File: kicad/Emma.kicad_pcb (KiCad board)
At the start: 4 copper layers, 55 x 35 mm, 78 parts, among them U1 ByA 100nF +3V3 U1-VDDA Bypass, U1 ByB 100nF +3V3 U1-VDD Bypass

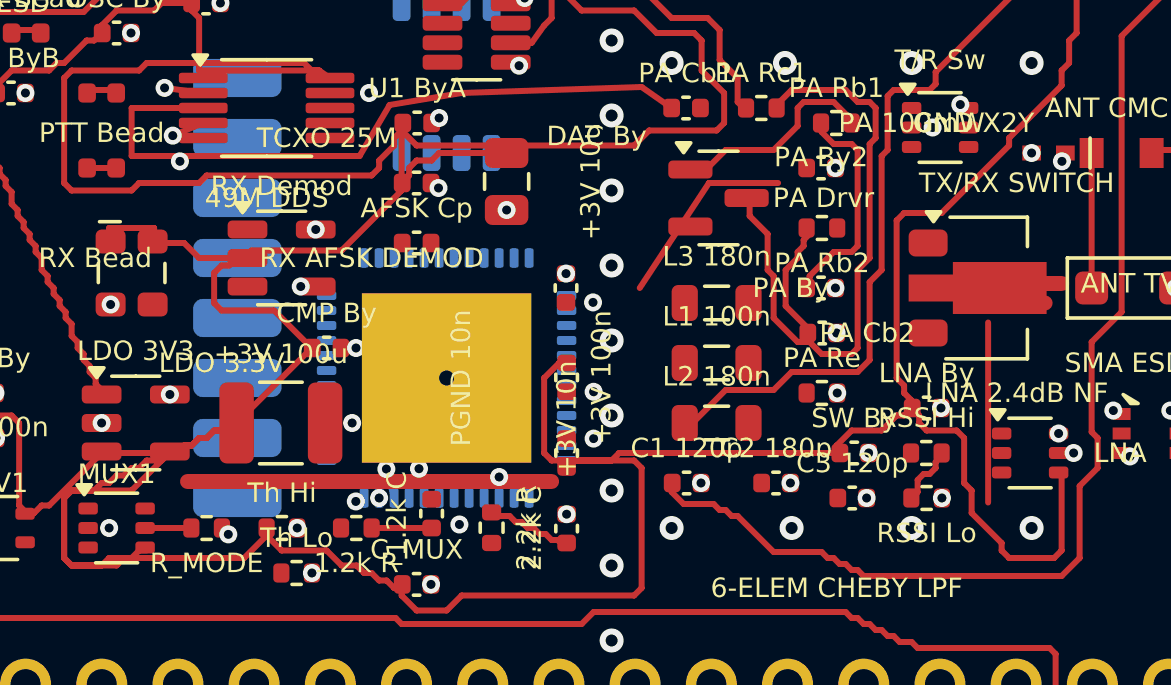
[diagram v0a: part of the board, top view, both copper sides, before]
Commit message: Clear Emma pre-existing DRC debt + schematic-parity so CI validator passes
Editing Emma.kicad_pcb pulled it into the CI KiCad validator's --changed-since
scope, which surfaced 35 pre-existing hard DRC violations plus 26 new
schematic-parity conflicts. All fixed at root cause (validator now reports
0 hard for Emma.kicad_sch ERC and Emma.kicad_pcb DRC):

- Schematic parity (26 net_conflict): gen_emma_sch.py now emits GLOBAL labels
  (bare net names match the PCB; local labels were named "/GND"). mod_emma_pcb.py
  assigns net-less pads the canonical "unconnected-(REF-PadN)" nets that the
  schematic no-connects generate.
- Solder-mask bridges (20): board solder-mask expansion was 0.10 mm (~2x normal),
  overlapping adjacent mask openings on 0.5 mm-pitch parts. cleanup_emma_drc.py
  sets it to the standard 0.05 mm.
- Clearance (15): POWER netclass clearance 0.20 -> 0.10 mm in Emma.kicad_pro
  (0.20 mm was over-conservative for a 5 V/3.3 V board and impossible for standard
  fine-pitch pads); the 4 real too-close auto-routed GND tracks deleted as
  redundant with the In1.Cu GND plane (GND connectivity unchanged: 23 -> 22
  unconnected).

Also black-formats cleanup_emma_drc.py; adds it to PROJECT_INDEX.md; updates
TODO.md. sch<->pcb parity remains exact.

Co-Authored-By: Claude Opus 4.8 <noreply@anthropic.com>
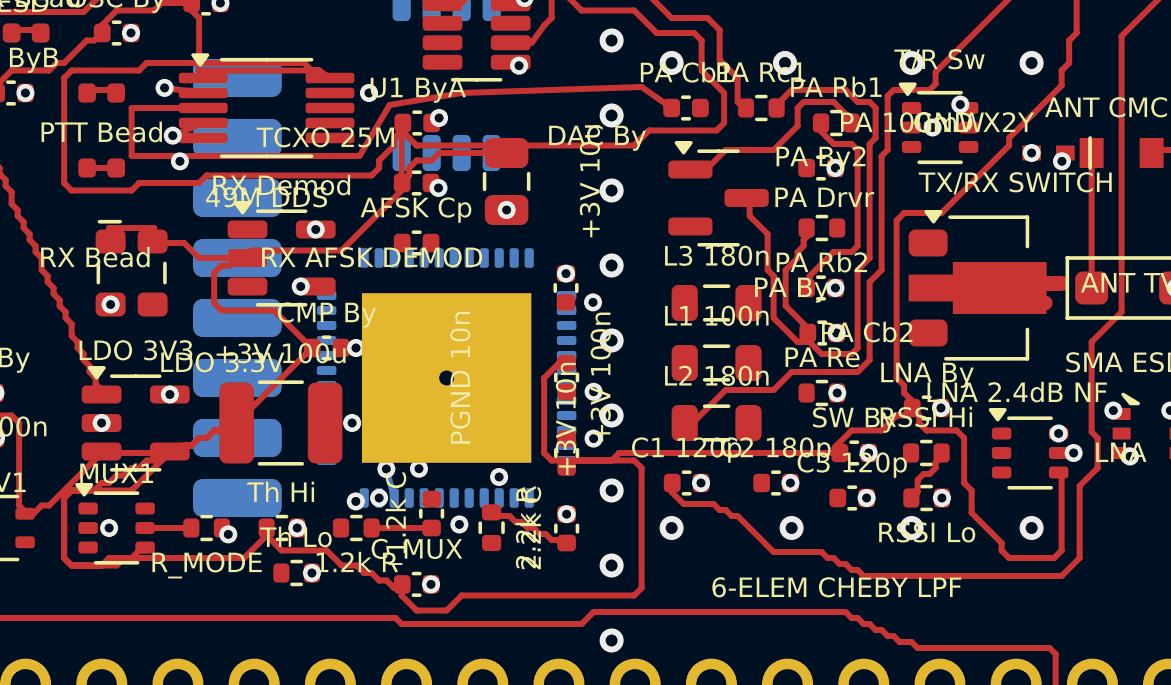
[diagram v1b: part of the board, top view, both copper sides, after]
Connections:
- ETH-PHY pad 13: (no net) -> unconnected-(ETH-PHY-Pad13)
- ETH-PHY pad 14: (no net) -> unconnected-(ETH-PHY-Pad14)
- ETH-PHY pad 15: (no net) -> unconnected-(ETH-PHY-Pad15)
- ETH-PHY pad 16: (no net) -> unconnected-(ETH-PHY-Pad16)
- ETH-PHY pad 17: (no net) -> unconnected-(ETH-PHY-Pad17)
- ETH-PHY pad 23: (no net) -> unconnected-(ETH-PHY-Pad23)
- ETH-PHY pad 24: (no net) -> unconnected-(ETH-PHY-Pad24)
- ETH-PHY pad 37: (no net) -> unconnected-(ETH-PHY-Pad37)
- ETH-PHY pad 38: (no net) -> unconnected-(ETH-PHY-Pad38)
- ETH-PHY pad 39: (no net) -> unconnected-(ETH-PHY-Pad39)
- ETH-PHY pad 42: (no net) -> unconnected-(ETH-PHY-Pad42)
- ETH-PHY pad 43: (no net) -> unconnected-(ETH-PHY-Pad43)
- ETH-PHY pad 44: (no net) -> unconnected-(ETH-PHY-Pad44)
- ETH-PHY pad 45: (no net) -> unconnected-(ETH-PHY-Pad45)
- ETH-PHY pad 46: (no net) -> unconnected-(ETH-PHY-Pad46)
- ETH-PHY pad 47: (no net) -> unconnected-(ETH-PHY-Pad47)
- ETH-PHY pad 48: (no net) -> unconnected-(ETH-PHY-Pad48)
- INV1 pad 5: (no net) -> unconnected-(INV1-Pad5)
- LoRa pad 11: (no net) -> unconnected-(LoRa-Pad11)
- LoRa pad 12: (no net) -> unconnected-(LoRa-Pad12)
- LoRa pad 13: (no net) -> unconnected-(LoRa-Pad13)
- LoRa pad 14: (no net) -> unconnected-(LoRa-Pad14)
- LoRa pad 15: (no net) -> unconnected-(LoRa-Pad15)
- LoRa pad 16: (no net) -> unconnected-(LoRa-Pad16)
- LoRa pad 7: (no net) -> unconnected-(LoRa-Pad7)
- LoRa pad 9: (no net) -> unconnected-(LoRa-Pad9)
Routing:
- net GND: track 33.9 -> 9.27 mm
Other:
- rule pad_to_mask_clearance: 0.1 -> 0.05

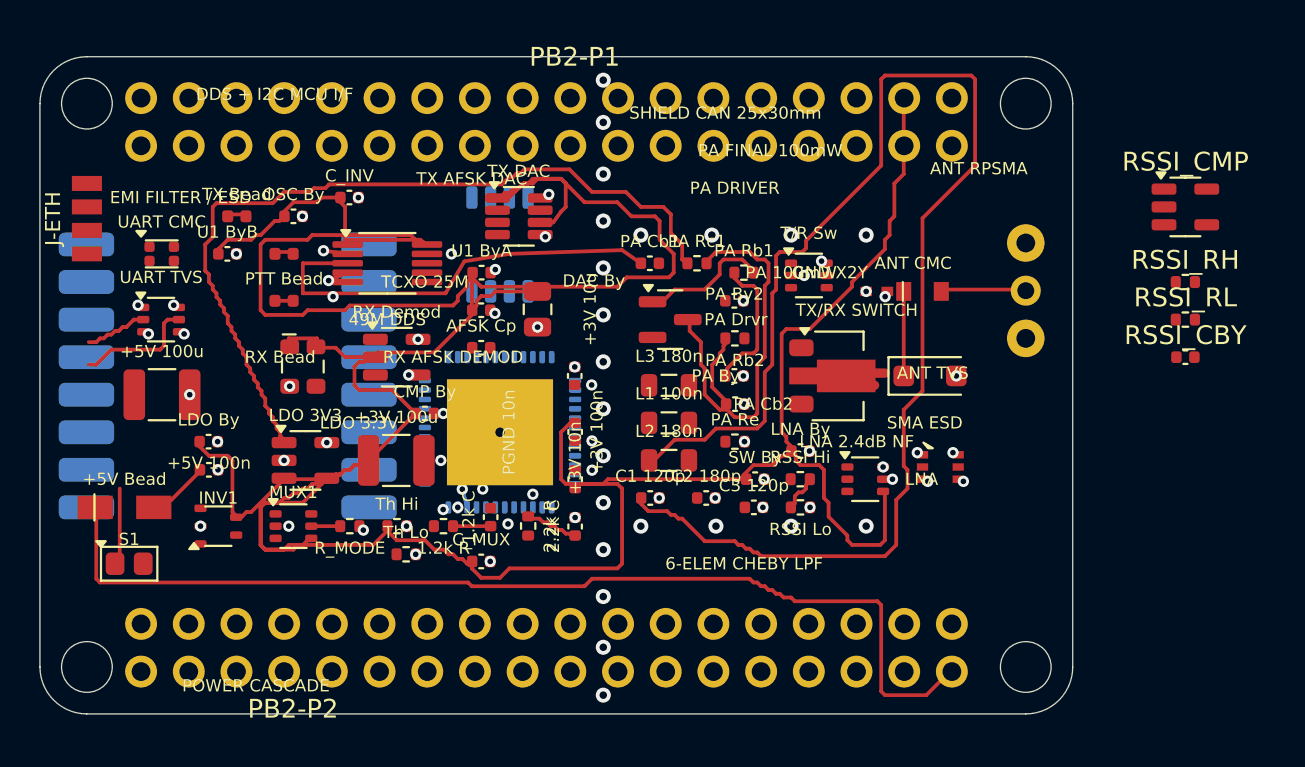
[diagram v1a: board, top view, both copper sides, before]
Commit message: Emma: route RSSI sub-circuit after user placement (0 hard DRC)
The user manually placed the 4 RSSI parts (RSSI_CMP + RSSI_RH/RL/CBY) on B.Cu in
the RF section and marked "NET validation, DRC & Routing" as the next step.

- Validated: sch<->pcb parity exact (refs + net sets match); the placement
  introduced 0 hard DRC violations (0 shorting/clearance/courtyard/solder-mask).
- Routed the sub-circuit via avionics/kicad/route_emma_rssi.py (pcbnew), DRC-tuned:
    GND      -> B.Cu tie of the 3 GND pads + one via to the F.Cu GND pour at RL.2
    RSSI_REF -> B.Cu weave through the 0.5 mm mid-channel around the wide CMP.4 pad
    +3V3     -> internal (RH.1/CBY.1/CMP.2) + board tie to LNA By
    RSSI_ANA -> CMP.1 -> RSSI Lo divider (B.Cu east + via)
  0.15 mm traces, 0.30 mm-drill/0.55 mm vias, zones refilled.
- Result: 0 hard DRC, 0 drill-out-of-range, parity intact; unconnected 104 -> 95.

Remaining: RSSI_DCD (RSSI_CMP.5 -> PB2-P2 pad 2) — a ~28 mm cross-board run through
the ETH-PHY/LoRa and PB2 header congestion; left for GUI push-shove / autorouter
(route_emma_rssi.py holds a starting attempt). Tracked in TODO.md §1.2b.

Also reverted a corrupted Vera.kicad_pcb (a GUI-save had rewritten its layer table
so it Failed to load; restored the committed version).

Co-Authored-By: Claude Opus 4.8 <noreply@anthropic.com>
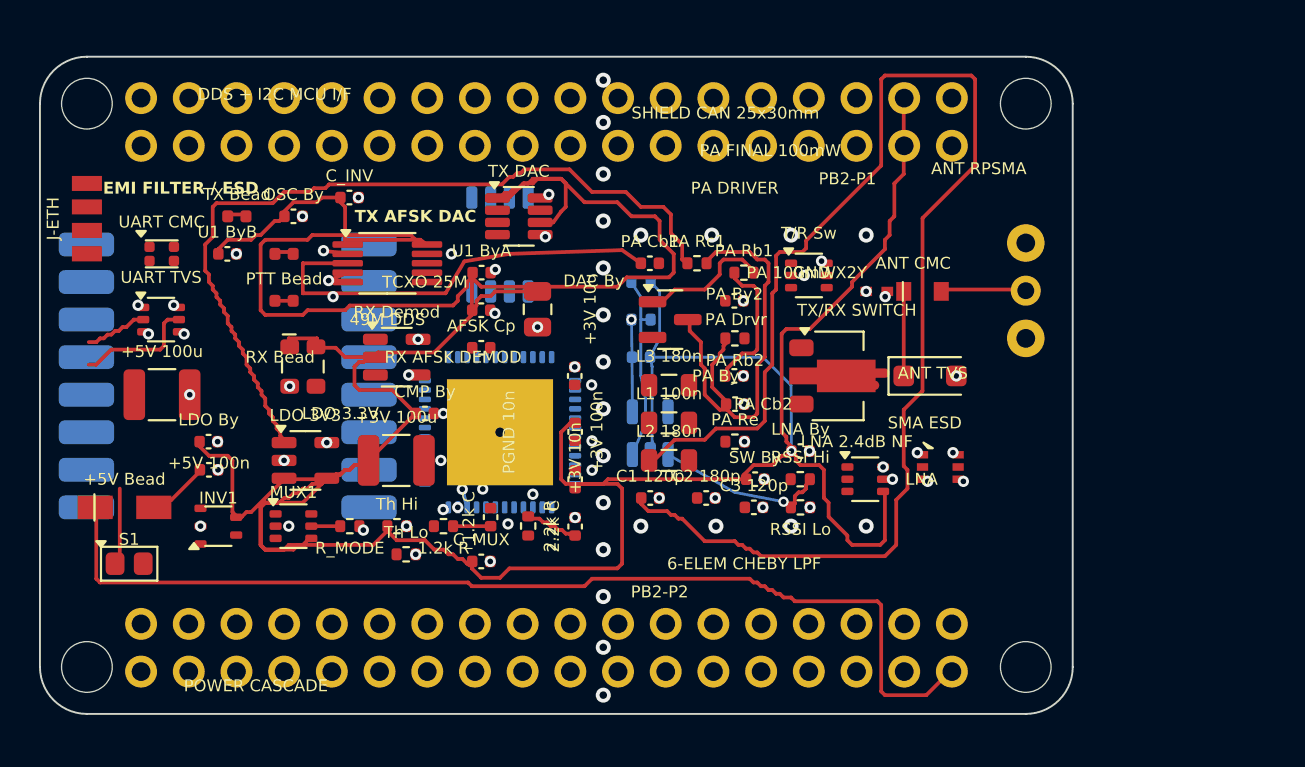
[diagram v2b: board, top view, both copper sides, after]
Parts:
- RSSI_CBY, RSSI_CMP, RSSI_RH, RSSI_RL: moved to B.Cu
- moved RSSI_CMP 30.9 mm to (132.5, 120.0), turned to 90 degrees
- moved RSSI_CBY 29.0 mm to (132.0, 116.0), turned to 180 degrees
- moved RSSI_RH 29.0 mm to (132.0, 112.0), turned to 180 degrees
- moved RSSI_RL 29.0 mm to (132.0, 114.0), turned to 180 degrees
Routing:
- net +3V3: track 214.7 -> 235.8 mm, vias 0 -> 1
- net RSSI_REF: track 0.00 -> 10.0 mm
- net RSSI_ANA: track 2.13 -> 9.35 mm, vias 0 -> 1
- net GND: track 9.27 -> 14.2 mm, vias 81 -> 82
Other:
- board text added: "DIGITAL SECT UART/pwr/modem"
- board text removed: "DIGITAL SECTION UART / power / modem"
